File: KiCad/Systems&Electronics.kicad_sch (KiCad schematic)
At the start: 22 parts, among them U1 HX711, U3 MAX485E, U4 MAX485E

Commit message: V1 Systems Schematics
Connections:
- net +12V: now also 5V Relay1. (NO), 5V Relay2. (NO), 5V Relay3. (NO)
- net -12V: now also 5V Relay1. (NO), 5V Relay2. (NO), 5V Relay3. (NO), A1.5V3 (5V), A1.GND1 (GND), A1.GND2 (GND), A1.GND3 (GND), A1.GND5 (GND), A1.GND6 (GND), Load_Cell1. (VCC), Pressure_Transducer1. (VCC), Pressure_Transducer2. (VCC), Pressure_Transducer3. (VCC), Pressure_Transducer4. (VCC), Pressure_Transducer5. (VCC), Pressure_Transducer6. (VCC), Solenoid1. (-), Solenoid2. (-), Solenoid3. (-), U1.16 (DVDD), U1.5 (AGND)
- net at A1.5V2 (SPI_5V): now also MAX6675_1. (VCC)
- net at A1.D22: now also 5V Relay1. (NO)
- net at A1.D23: now also 5V Relay2. (NO)
- net at A1.D24: now also 5V Relay3. (NO)
- net at A1.D25: now also MAX6675_1. (VCC)
- net at A1.D26: now also U1.12 (DOUT)
- net at A1.D27: now also U1.11 (PD_SCK)
- net at A1.GND4 (SPI_GND): now also MAX6675_1. (VCC)
- net at A1.MISO (SPI_MISO): now also MAX6675_1. (VCC)
- net at A1.SCK (SPI_SCK): now also MAX6675_1. (VCC)
- net at MAX6675_1. (VCC): now also Thermocouple1. (-)
- net at U1.1 (VSUP): now also Load_Cell1. (VCC)
- net at U1.7 (INA-): now also Load_Cell1. (VCC)
- net at U1.8 (INA+): now also Load_Cell1. (VCC)
- new net: 5V Relay1. (NO), Solenoid1. (-)
- new net: 5V Relay3. (NO), Solenoid3. (-)
- new net: 5V Relay2. (NO), Solenoid2. (-)
- new net: MAX6675_1. (VCC), Thermocouple1. (-)
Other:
- moved on the sheet: 5V Relay1, 5V Relay2, 5V Relay3, Solenoid1, Solenoid2, Solenoid3

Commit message: Electronics Schematic V1.1.0
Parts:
- removed U1: HX711, Package_SO:SOP-16_3.9x9.9mm_P1.27mm, symbol Analog_ADC:HX711
- added HX711_Board1: ~, symbol Sensors:HX711_Board
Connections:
- net +12V: now also A1.VIN
- net -12V: no longer 5V Relay1. (NO), 5V Relay2. (NO), 5V Relay3. (NO), A1.5V3 (5V), A1.GND1 (GND), A1.GND3 (GND), A1.GND5 (GND), A1.GND6 (GND), Load_Cell1. (VCC), Pressure_Transducer1. (VCC), Pressure_Transducer2. (VCC), Pressure_Transducer3. (VCC), Pressure_Transducer4. (VCC), Pressure_Transducer5. (VCC), Pressure_Transducer6. (VCC), Solenoid1. (-), Solenoid2. (-), Solenoid3. (-)
- net at A1.D22: now also MAX6675_1. (VCC); no longer 5V Relay1. (NO)
- net at Solenoid1. (-): now also A1.GND5 (GND), Solenoid2. (-), Solenoid3. (-); no longer 5V Relay1. (NO)
- net at A1.3V3 (3.3V): now also HX711_Board1. (VCC)
- net at A1.5V4 (5V): now also 5V Relay1. (NO), 5V Relay2. (NO), 5V Relay3. (NO)
- net at A1.A0: now also Pressure_Transducer1. (VCC)
- net at A1.A1: now also Pressure_Transducer2. (VCC)
- net at A1.A2: now also Pressure_Transducer3. (VCC)
- net at A1.A3: now also Pressure_Transducer4. (VCC)
- net at A1.A4: now also Pressure_Transducer5. (VCC)
- net at A1.A5: now also Pressure_Transducer6. (VCC)
- net at A1.D23: now also HX711_Board1. (VCC); no longer 5V Relay2. (NO)
- net at A1.D24: now also HX711_Board1. (VCC); no longer 5V Relay3. (NO)
- net at A1.D25: now also 5V Relay1. (NO); no longer MAX6675_1. (VCC)
- net at A1.D26: now also 5V Relay2. (NO)
- net at A1.D27: now also 5V Relay3. (NO)
- net at Pressure_Transducer2. (VCC): now also A1.GND1 (GND), Pressure_Transducer1. (VCC), Pressure_Transducer3. (VCC), Pressure_Transducer4. (VCC), Pressure_Transducer5. (VCC), Pressure_Transducer6. (VCC)
- net at Load_Cell1. (VCC): now also HX711_Board1. (VCC)
- new net: 5V Relay1. (NO), 5V Relay2. (NO), 5V Relay3. (NO), A1.GND3 (GND)
- new net: 5V Relay1. (NO), Solenoid1. (-)
- new net: A1.5V3 (5V), Pressure_Transducer1. (VCC), Pressure_Transducer2. (VCC), Pressure_Transducer3. (VCC), Pressure_Transducer4. (VCC), Pressure_Transducer5. (VCC), Pressure_Transducer6. (VCC)
- new net: A1.GND6 (GND), HX711_Board1. (VCC)
- new net: HX711_Board1. (VCC), Load_Cell1. (VCC) (x3)
- new net: MAX6675_1. (VCC), Thermocouple1. (-)
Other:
- note added: "1.1.0"
- note added: "August 7, 2024"
- note added: "MAX6675_1"
- note removed: "1.0.0"
- note removed: "July 22nd, 2024"
- moved on the sheet: 5V Relay1, 5V Relay2, 5V Relay3, Load_Cell1, Solenoid1, Solenoid2, Solenoid3, Thermocouple1

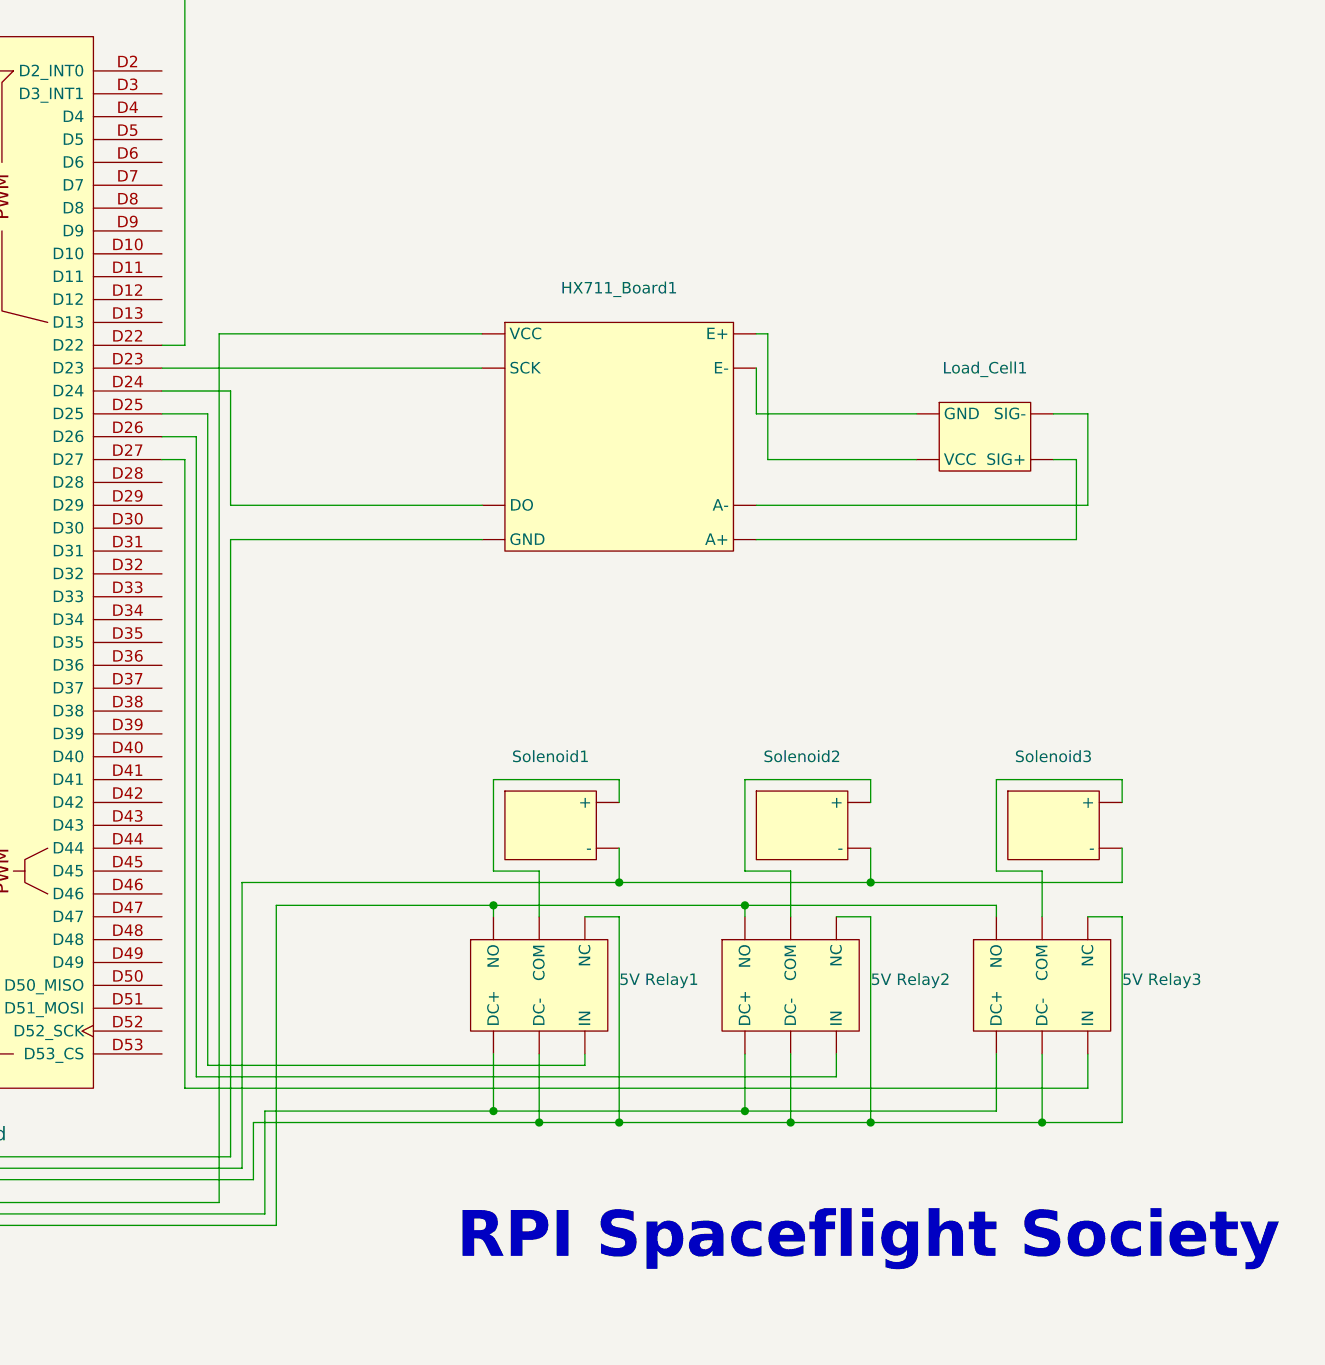
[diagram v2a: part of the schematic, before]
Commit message: Adding Igniter to Schematic
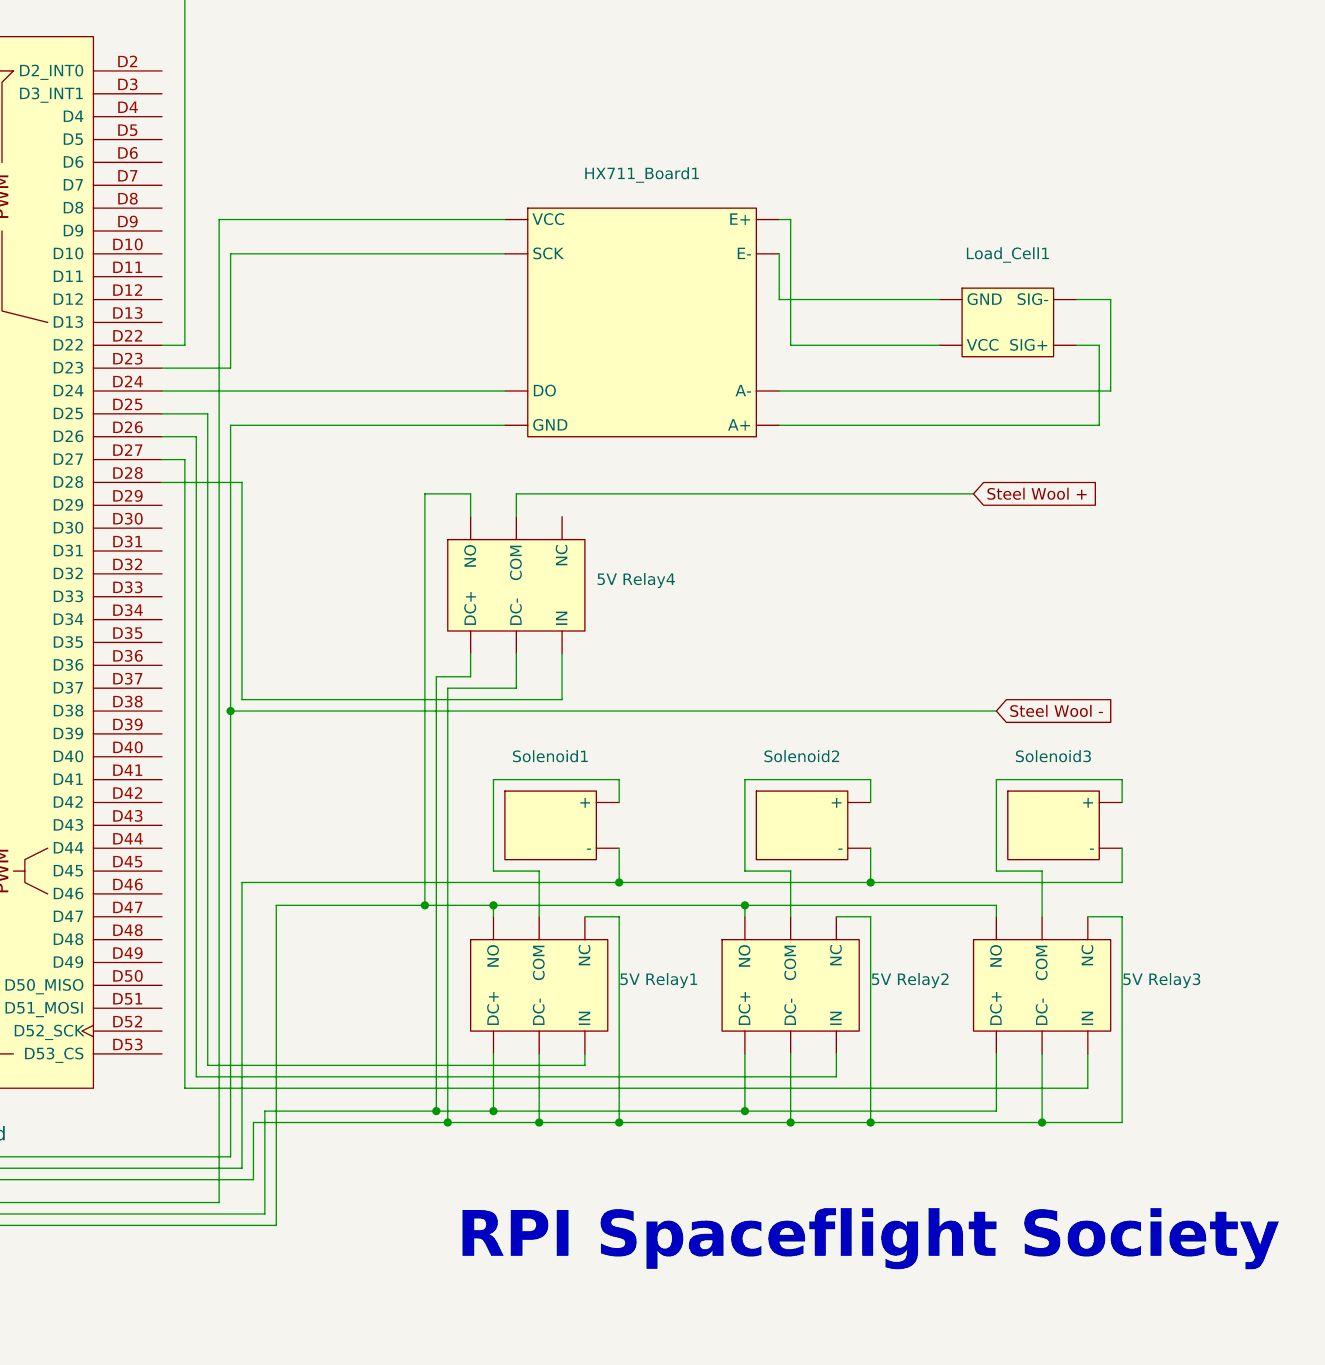
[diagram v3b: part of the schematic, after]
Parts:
- added 5V Relay4: ~, symbol 5VRelay:5V_Relay
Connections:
- net +12V: now also 5V Relay4. (NO)
- net at Solenoid1. (-): now also A1.GND5 (GND), Solenoid2. (-), Solenoid3. (-); no longer 5V Relay1. (NO)
- net at Pressure_Transducer1. (VCC), Pressure_Transducer2. (VCC), Pressure_Transducer3. (VCC)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: now also A1.GND1 (GND); no longer A1.5V3 (5V)
- net at A1.D28: now also 5V Relay4. (NO)
- net Steel Wool -: now reaches A1.GND6 (GND), HX711_Board1. (VCC)
- new net: 5V Relay1. (NO), 5V Relay2. (NO), 5V Relay3. (NO), 5V Relay4. (NO), A1.5V4 (5V)
- new net: 5V Relay1. (NO), 5V Relay2. (NO), 5V Relay3. (NO), 5V Relay4. (NO), A1.GND3 (GND)
- new net: 5V Relay1. (NO), Solenoid1. (-)
- new net: A1.5V3 (5V), Pressure_Transducer1. (VCC), Pressure_Transducer2. (VCC), Pressure_Transducer3. (VCC), Pressure_Transducer4. (VCC), Pressure_Transducer5. (VCC), Pressure_Transducer6. (VCC)
- new net: HX711_Board1. (VCC), Load_Cell1. (VCC) (x3)
- new net: MAX6675_1. (VCC), Thermocouple1. (-)
- new net Steel Wool +: 5V Relay4. (NO)
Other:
- moved on the sheet: HX711_Board1, Load_Cell1

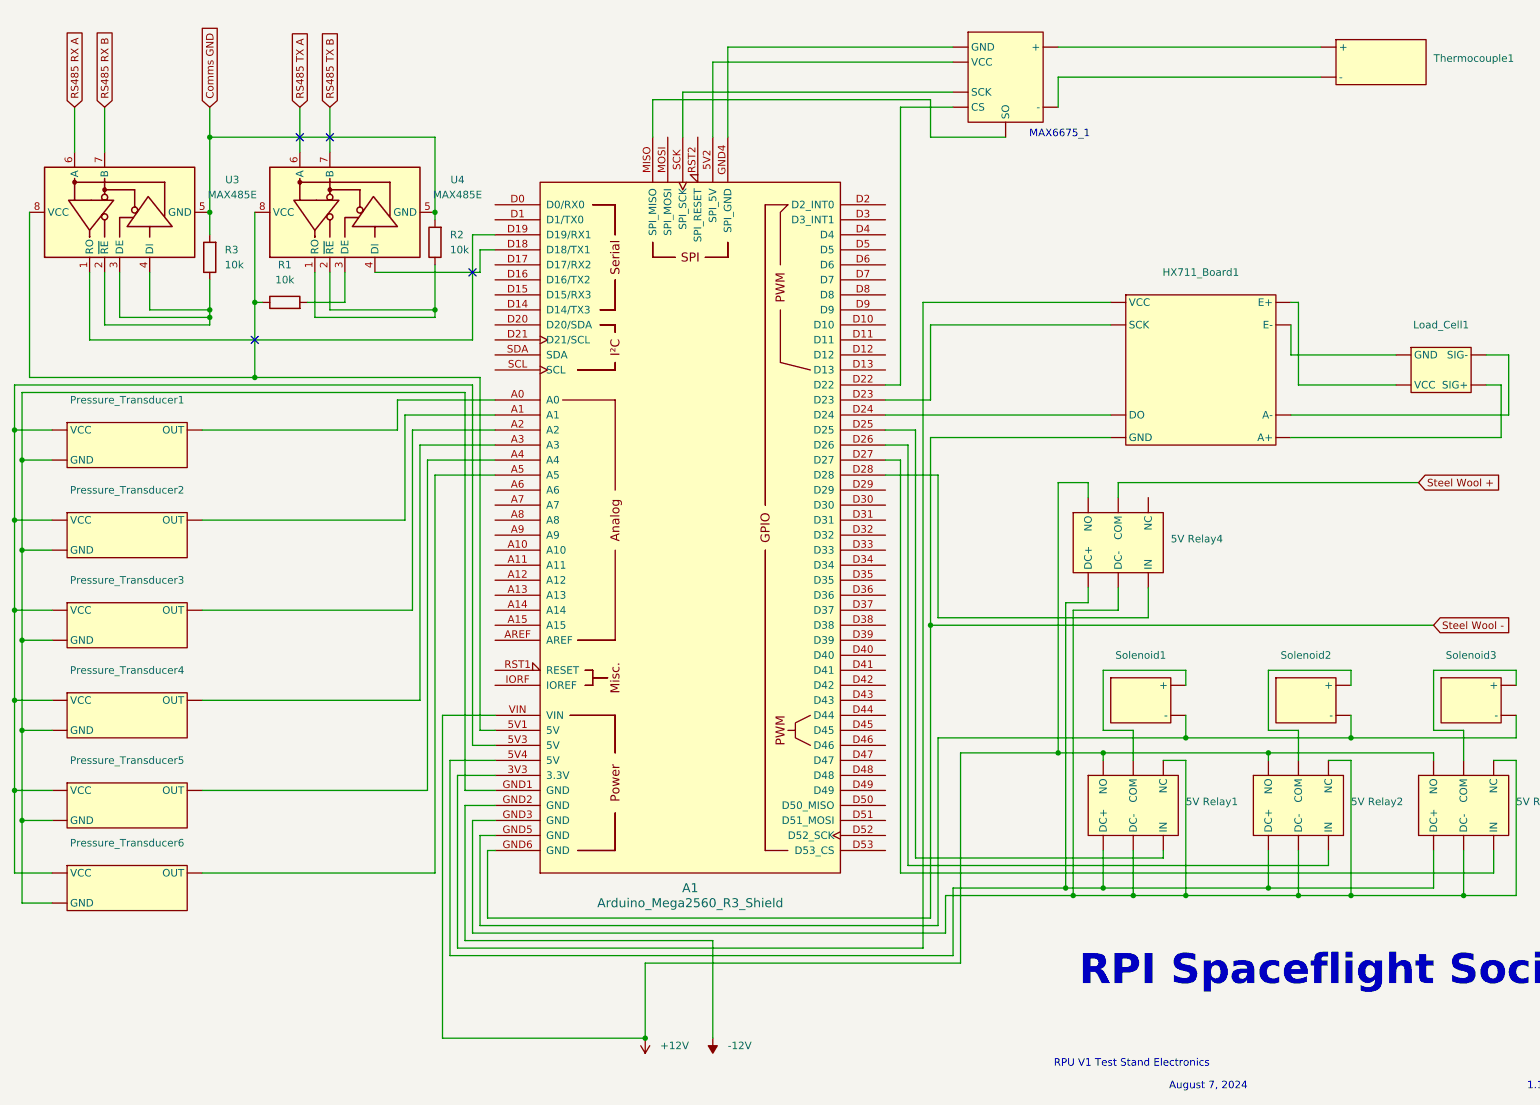
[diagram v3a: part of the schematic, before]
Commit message: fix: Adding Resistors, Capacitors, and Diodes to Schematic - Also rerouted 12v ground to not run through the Arduino
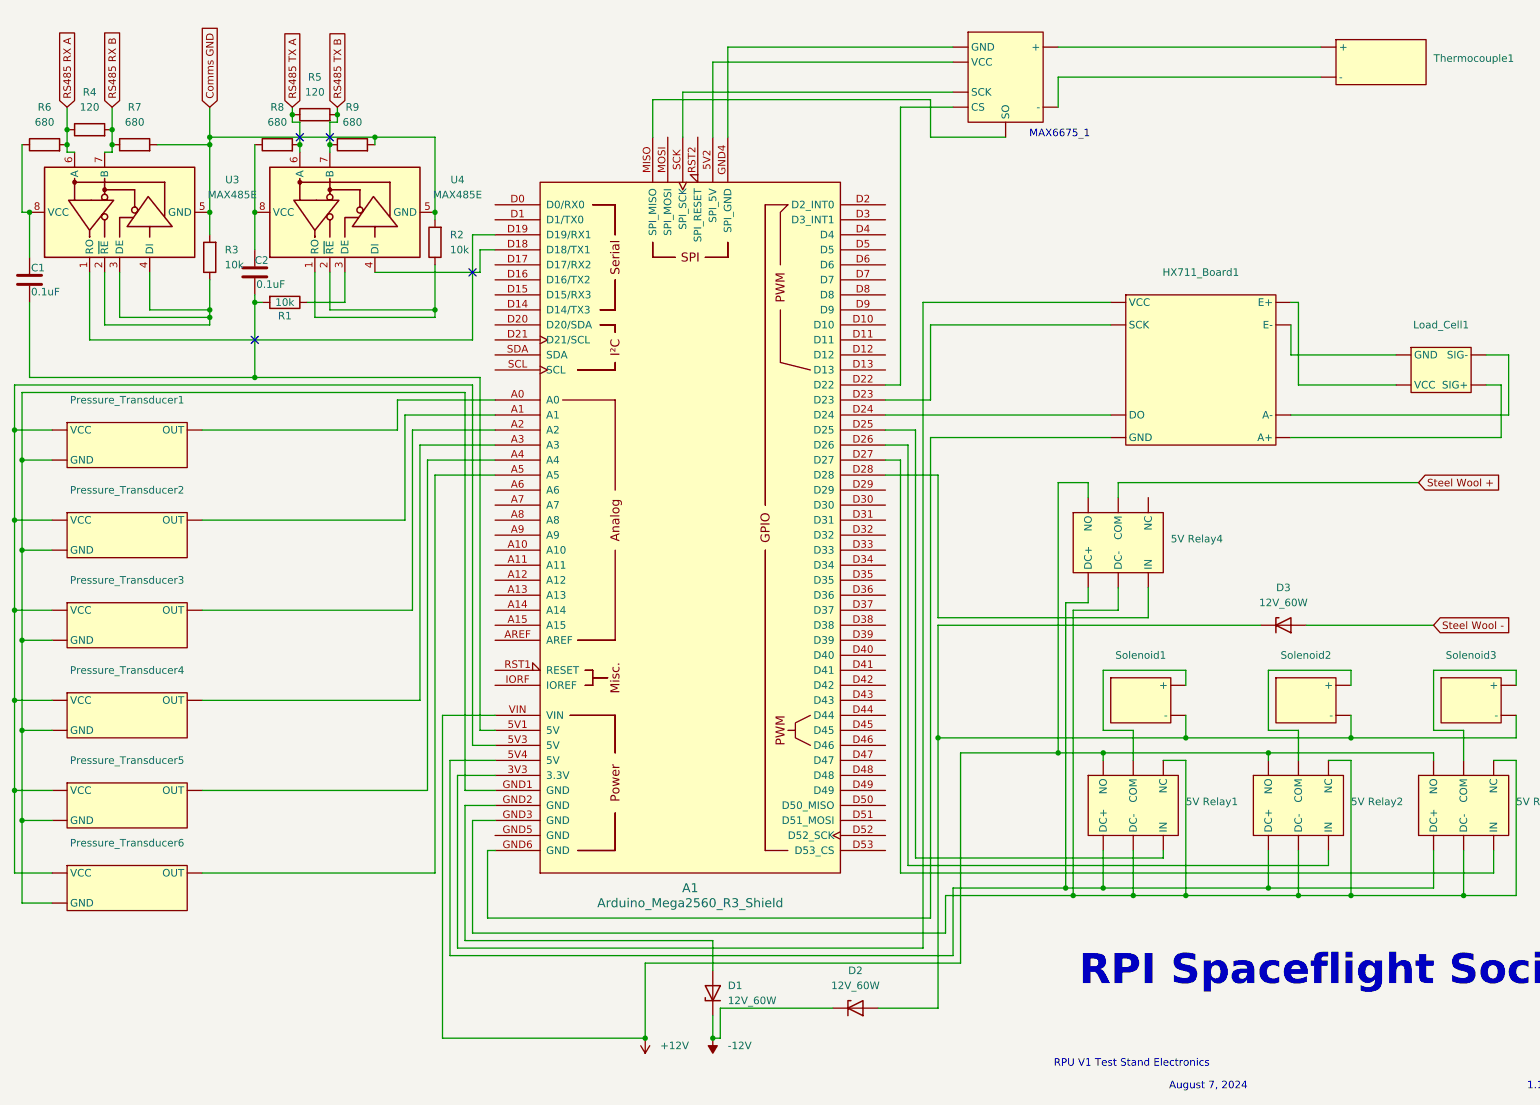
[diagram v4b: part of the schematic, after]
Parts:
- added C1, C2: 0.1uF, symbol Device:C
- added D1, D2, D3: 12V_60W, Diode_SMD:Nexperia_DSN1608-2_1.6x0.8mm, symbol Diode:PTVS12VZ1USK
- added R4, R5: 120, symbol Device:R
- added R6, R7, R8, R9: 680, symbol Device:R
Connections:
- net -12V: now also D1.1 (K), D2.1 (K); no longer A1.GND2 (GND)
- net Comms GND: now also R7.2, R9.2
- net RS485 RX A: now also R4.1, R6.2
- net RS485 RX B: now also R4.2, R7.1
- net RS485 TX A: now also R5.1, R8.2
- net RS485 TX B: now also R5.2, R9.1
- net Steel Wool -: now also D3.2 (A); no longer A1.GND6 (GND), HX711_Board1. (VCC)
- net at Solenoid1. (-): now also Solenoid2. (-), Solenoid3. (-), D2.2 (A), D3.1 (K); no longer 5V Relay1. (NO)
- net at Pressure_Transducer1. (VCC), Pressure_Transducer2. (VCC), Pressure_Transducer3. (VCC)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: now also A1.GND1 (GND); no longer A1.5V3 (5V)
- net at R1.2: now also A1.5V1 (5V), C1.2, C2.1; no longer U4.3 (DE)
- new net: C1.1, R6.1, U3.8 (VCC)
- new net: C2.2, R8.1, U4.8 (VCC)
- new net: 5V Relay1. (NO), 5V Relay2. (NO), 5V Relay3. (NO), 5V Relay4. (NO), A1.5V4 (5V)
- new net: 5V Relay1. (NO), 5V Relay2. (NO), 5V Relay3. (NO), 5V Relay4. (NO), A1.GND3 (GND)
- new net: 5V Relay1. (NO), Solenoid1. (-)
- new net: A1.5V3 (5V), Pressure_Transducer1. (VCC), Pressure_Transducer2. (VCC), Pressure_Transducer3. (VCC), Pressure_Transducer4. (VCC), Pressure_Transducer5. (VCC), Pressure_Transducer6. (VCC)
- new net: A1.GND2 (GND), D1.2 (A)
- new net: A1.GND6 (GND), HX711_Board1. (VCC)
- new net: R1.1, U4.3 (DE)
- new net: HX711_Board1. (VCC), Load_Cell1. (VCC) (x3)
- new net: 5V Relay3. (NO), Solenoid3. (-)
- new net: MAX6675_1. (VCC), Thermocouple1. (-)
- now unconnected: A1.GND5 (GND)
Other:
- moved on the sheet: R1
